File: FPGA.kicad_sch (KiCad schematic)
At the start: 115 parts, among them U7 CAT24C128, U8 LFE5U-25F-8MG285C, U9 W25Q128JVP

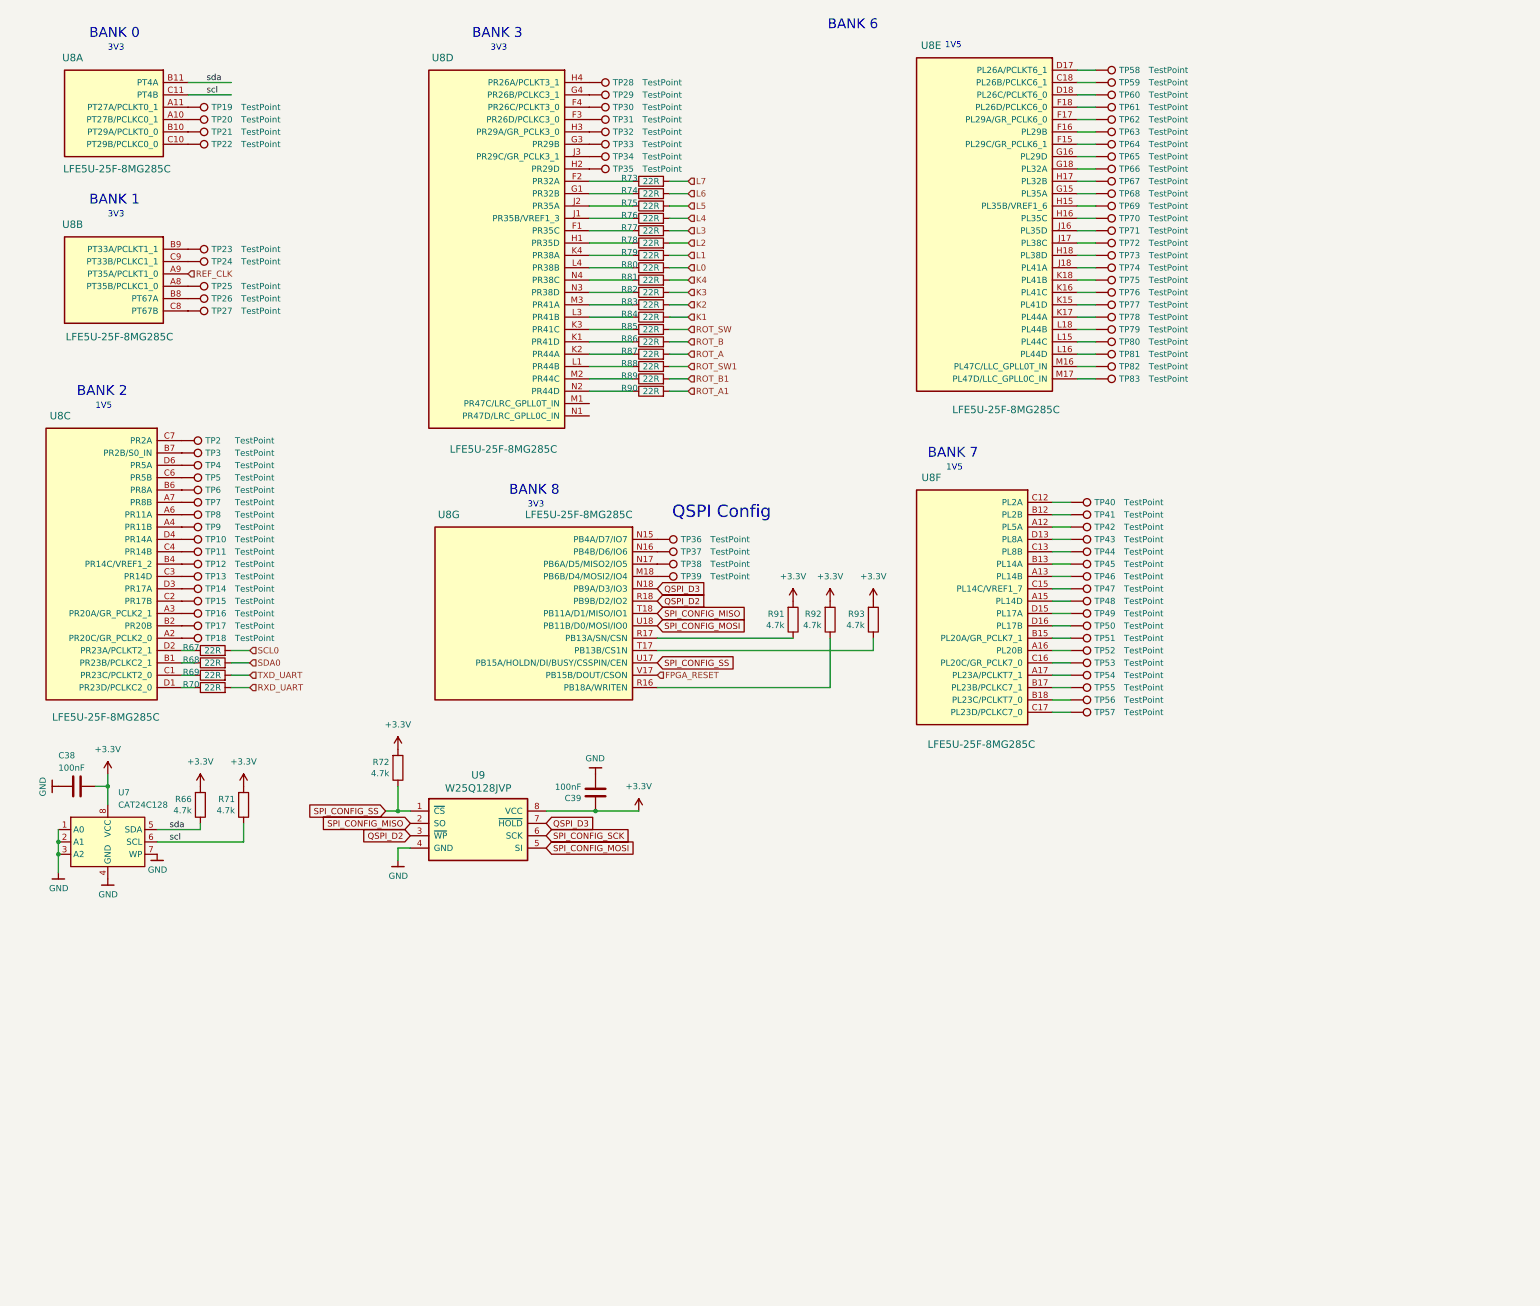
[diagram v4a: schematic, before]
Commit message: Add sram and oscillator 27MHz
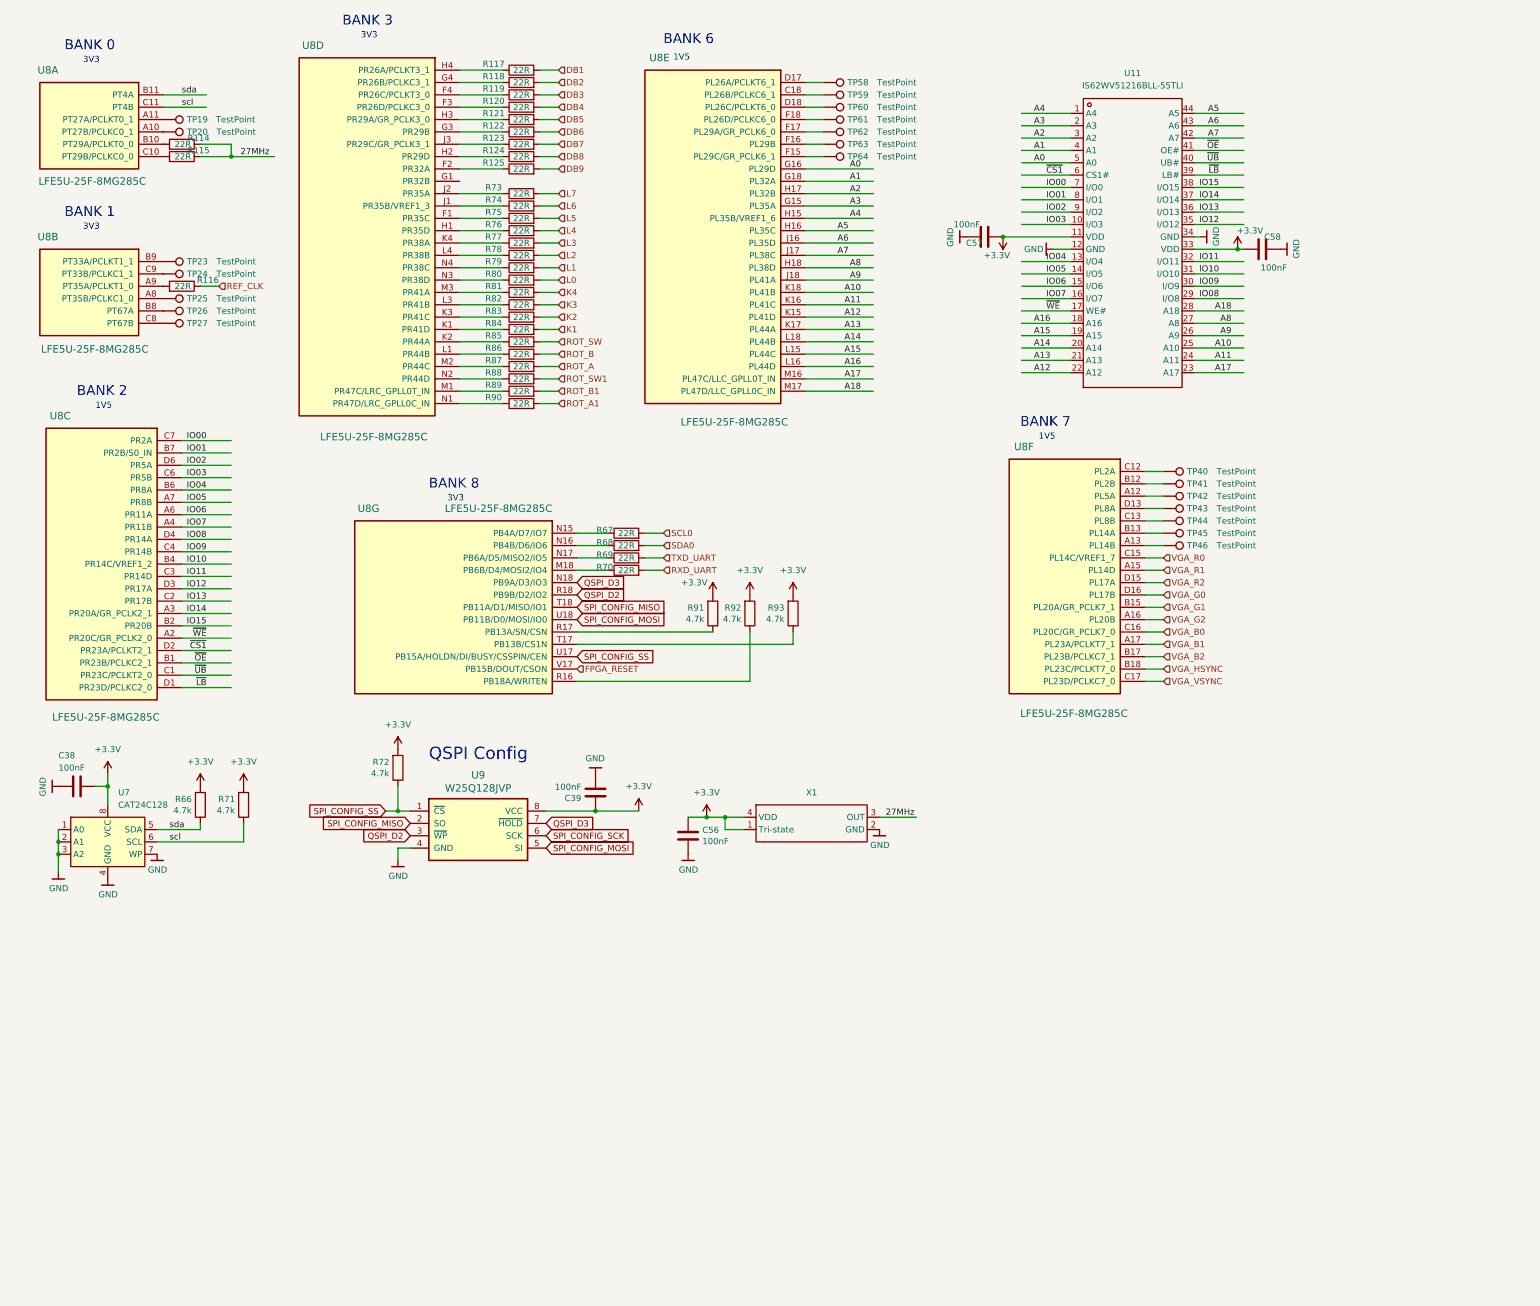
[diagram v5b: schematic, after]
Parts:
- removed TP10, TP11, TP12, TP13, TP14, TP15, TP16, TP17, TP18, TP2, TP21, TP22, TP28, TP29, TP3, TP30, TP31, TP32, TP33, TP34, TP35, TP36, TP37, TP38, TP39, TP4, TP47, TP48, TP49, TP5, TP50, TP51, TP52, TP53, TP54, TP55, TP56, TP57, TP6, TP65, TP66, TP67, TP68, TP69, TP7, TP70, TP71, TP72, TP73, TP74, TP75, TP76, TP77, TP78, TP79, TP8, TP80, TP81, TP82, TP83, TP9: TestPoint, TestPoint:TestPoint_THTPad_D1.5mm_Drill0.7mm, symbol Connector:TestPoint
- added C56, C57, C58: 100nF, Capacitor_SMD:C_0603_1608Metric, symbol Device:C
- added R114, R115, R116, R117, R118, R119, R120, R121, R122, R123, R124, R125: 22R, Resistor_SMD:R_0603_1608Metric, symbol Device:R
- added U11: IS62WV51216BLL-55TLI, EasyEDA_Lib:TSOP-44_L18.4-W10.2-P0.80-LS11.8-BL, symbol EasyEDA_Lib:IS62WV51216BLL-55TLI
- added X1: 27MHz, EasyEDA_Lib:OSC-SMD_4P-L3.2-W2.5-BL, symbol EasyEDA_Lib:OT2EL4C4JI-111OLP-27M
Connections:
- net +3.3V: now also C56.1, C57.1, C58.1, U11.11 (VDD), U11.33 (VDD), X1.1 (Tri-state), X1.4 (VDD)
- net GND: now also C56.2, C57.2, C58.2, U11.12 (GND), U11.34 (GND), X1.2 (GND)
- net REF_CLK: now also R116.1; no longer U8.A9 (PT35A/PCLKT1_0)
- net at U8.B10 (PT29A/PCLKT0_0): now also R114.2
- net at U8.C10 (PT29B/PCLKC0_0): now also R115.2
- net ~{WE}: now reaches U8.A2 (PR20C/GR_PCLK2_0)
- net ~{WE}: now also U11.17 (WE#)
- net IO14: now reaches U8.A3 (PR20A/GR_PCLK2_1)
- net IO14: now also U11.37 (I/O14)
- net IO07: now reaches U8.A4 (PR11B)
- net IO07: now also U11.16 (I/O7)
- net IO06: now reaches U8.A6 (PR11A)
- net IO06: now also U11.15 (I/O6)
- net IO05: now reaches U8.A7 (PR8B)
- net IO05: now also U11.14 (I/O5)
- net at R68.1: now also U8.N16 (PB4B/D6/IO6); no longer U8.B1 (PR23B/PCLKC2_1)
- net IO15: now reaches U8.B2 (PR20B)
- net IO15: now also U11.38 (I/O15)
- net IO10: now reaches U8.B4 (PR14C/VREF1_2)
- net IO10: now also U11.31 (I/O10)
- net IO04: now reaches U8.B6 (PR8A)
- net IO04: now also U11.13 (I/O4)
- net IO01: now reaches U8.B7 (PR2B/S0_IN)
- net IO01: now also U11.8 (I/O1)
- net at R69.1: now also U8.N17 (PB6A/D5/MISO2/IO5); no longer U8.C1 (PR23C/PCLKT2_0)
- net IO13: now reaches U8.C2 (PR17B)
- net IO13: now also U11.36 (I/O13)
- net IO11: now reaches U8.C3 (PR14D)
- net IO11: now also U11.32 (I/O11)
- net IO09: now reaches U8.C4 (PR14B)
- net IO09: now also U11.30 (I/O9)
- net IO03: now reaches U8.C6 (PR5B)
- net IO03: now also U11.10 (I/O3)
- net IO00: now reaches U8.C7 (PR2A)
- net IO00: now also U11.7 (I/O0)
- net at R70.1: now also U8.M18 (PB6B/D4/MOSI2/IO4); no longer U8.D1 (PR23D/PCLKC2_0)
- net at R67.1: now also U8.N15 (PB4A/D7/IO7); no longer U8.D2 (PR23A/PCLKT2_1)
- net IO12: now reaches U8.D3 (PR17A)
- net IO12: now also U11.35 (I/O12)
- net IO08: now reaches U8.D4 (PR14A)
- net IO08: now also U11.29 (I/O8)
- net IO02: now reaches U8.D6 (PR5A)
- net IO02: now also U11.9 (I/O2)
- net at U8.F1 (PR35C): now also R75.1; no longer R77.1
- net at U8.F2 (PR32A): now also R125.1; no longer R73.1
- net at U8.F3 (PR26D/PCLKC3_0): now also R120.1
- net at U8.F4 (PR26C/PCLKT3_0): now also R119.1
- net at U8.G1 (PR32B): no longer R74.1
- net at U8.G3 (PR29B): now also R122.1
- net at U8.G4 (PR26B/PCLKC3_1): now also R118.1
- net at U8.H1 (PR35D): now also R76.1; no longer R78.1
- net at U8.H2 (PR29D): now also R124.1
- net at U8.H3 (PR29A/GR_PCLK3_0): now also R121.1
- net at U8.H4 (PR26A/PCLKT3_1): now also R117.1
- net at U8.J1 (PR35B/VREF1_3): now also R74.1; no longer R76.1
- net at U8.J2 (PR35A): now also R73.1; no longer R75.1
- net at U8.J3 (PR29C/GR_PCLK3_1): now also R123.1
- net at U8.K1 (PR41D): now also R84.1; no longer R86.1
- net at U8.K2 (PR44A): now also R85.1; no longer R87.1
- net at U8.K3 (PR41C): now also R83.1; no longer R85.1
- net at U8.K4 (PR38A): now also R77.1; no longer R79.1
- net at U8.L1 (PR44B): now also R86.1; no longer R88.1
- net at U8.L3 (PR41B): now also R82.1; no longer R84.1
- net at U8.L4 (PR38B): now also R78.1; no longer R80.1
- net at U8.M1 (PR47C/LRC_GPLL0T_IN): now also R89.1
- net at U8.M2 (PR44C): now also R87.1; no longer R89.1
- net at U8.M3 (PR41A): now also R81.1; no longer R83.1
- net at U8.N1 (PR47D/LRC_GPLL0C_IN): now also R90.1
- net at U8.N2 (PR44D): now also R88.1; no longer R90.1
- net at U8.N3 (PR38D): now also R80.1; no longer R82.1
- net at U8.N4 (PR38C): now also R79.1; no longer R81.1
- net A3: now reaches U8.G15 (PL35A)
- net A3: now also U11.2 (A3)
- net A0: now reaches U8.G16 (PL29D)
- net A0: now also U11.5 (A0)
- net A1: now reaches U8.G18 (PL32A)
- net A1: now also U11.4 (A1)
- net A4: now reaches U8.H15 (PL35B/VREF1_6)
- net A4: now also U11.1 (A4)
- net A5: now reaches U8.H16 (PL35C)
- net A5: now also U11.44 (A5)
- net A2: now reaches U8.H17 (PL32B)
- net A2: now also U11.3 (A2)
- net A8: now reaches U8.H18 (PL38D)
- net A8: now also U11.27 (A8)
- net A6: now reaches U8.J16 (PL35D)
- net A6: now also U11.43 (A6)
- net A7: now reaches U8.J17 (PL38C)
- net A7: now also U11.42 (A7)
- net A9: now reaches U8.J18 (PL41A)
- net A9: now also U11.26 (A9)
- net A12: now reaches U8.K15 (PL41D)
- net A12: now also U11.22 (A12)
- net A11: now reaches U8.K16 (PL41C)
- net A11: now also U11.24 (A11)
- net A13: now reaches U8.K17 (PL44A)
- net A13: now also U11.21 (A13)
- net A10: now reaches U8.K18 (PL41B)
- net A10: now also U11.25 (A10)
- net A15: now reaches U8.L15 (PL44C)
- net A15: now also U11.19 (A15)
- net A16: now reaches U8.L16 (PL44D)
- net A16: now also U11.18 (A16)
- net A14: now reaches U8.L18 (PL44B)
- net A14: now also U11.20 (A14)
- net A17: now reaches U8.M16 (PL47C/LLC_GPLL0T_IN)
- net A17: now also U11.23 (A17)
- net A18: now reaches U8.M17 (PL47D/LLC_GPLL0C_IN)
- net A18: now also U11.28 (A18)
- net VGA_R1: now reaches U8.A15 (PL14D)
- net VGA_G2: now reaches U8.A16 (PL20B)
- net VGA_B1: now reaches U8.A17 (PL23A/PCLKT7_1)
- net VGA_G1: now reaches U8.B15 (PL20A/GR_PCLK7_1)
- net VGA_B2: now reaches U8.B17 (PL23B/PCLKC7_1)
- net VGA_HSYNC: now reaches U8.B18 (PL23C/PCLKT7_0)
- net VGA_R0: now reaches U8.C15 (PL14C/VREF1_7)
- net VGA_B0: now reaches U8.C16 (PL20C/GR_PCLK7_0)
- net VGA_VSYNC: now reaches U8.C17 (PL23D/PCLKC7_0)
- net VGA_R2: now reaches U8.D15 (PL17A)
- net VGA_G0: now reaches U8.D16 (PL17B)
- new net: R116.2, U8.A9 (PT35A/PCLKT1_0)
- new net 27MHz: R114.1, R115.1, X1.3 (OUT)
- new net DB1: R117.2
- new net DB2: R118.2
- new net DB3: R119.2
- new net DB4: R120.2
- new net DB5: R121.2
- new net DB6: R122.2
- new net DB7: R123.2
- new net DB8: R124.2
- new net DB9: R125.2
- new net ~{CS1}: U11.6 (CS1#), U8.D2 (PR23A/PCLKT2_1)
- new net ~{LB}: U11.39 (LB#), U8.D1 (PR23D/PCLKC2_0)
- new net ~{OE}: U11.41 (OE#), U8.B1 (PR23B/PCLKC2_1)
- new net ~{UB}: U11.40 (UB#), U8.C1 (PR23C/PCLKT2_0)
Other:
- moved on the sheet: R67, R68, R69, R70, R73, R74, R75, R76, R77, R78, R79, R80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

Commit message: Routing sram
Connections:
- net A2: now also U8.F18 (PL26D/PCLKC6_0); no longer U8.H17 (PL32B)
- net A3: no longer U8.G15 (PL35A)
- net A4: now also U8.A17 (PL23A/PCLKT7_1); no longer U8.H15 (PL35B/VREF1_6)
- net A6: now also U8.B17 (PL23B/PCLKC7_1); no longer U8.J16 (PL35D)
- net A7: now also U8.B15 (PL20A/GR_PCLK7_1); no longer U8.J17 (PL38C)
- net IO13: now also U8.G15 (PL35A); no longer U8.C2 (PR17B)
- net IO14: now also U8.F15 (PL29C/GR_PCLK6_1); no longer U8.A3 (PR20A/GR_PCLK2_1)
- net IO15: now also U8.D16 (PL17B); no longer U8.B2 (PR20B)
- net VGA_B0: no longer U8.C16 (PL20C/GR_PCLK7_0)
- net VGA_B1: no longer U8.A17 (PL23A/PCLKT7_1)
- net VGA_B2: no longer U8.B17 (PL23B/PCLKC7_1)
- net VGA_G0: no longer U8.D16 (PL17B)
- net VGA_G1: no longer U8.B15 (PL20A/GR_PCLK7_1)
- net VGA_G2: no longer U8.A16 (PL20B)
- net VGA_HSYNC: no longer U8.B18 (PL23C/PCLKT7_0)
- net VGA_R0: no longer U8.C15 (PL14C/VREF1_7)
- net VGA_R1: no longer U8.A15 (PL14D)
- net VGA_R2: no longer U8.D15 (PL17A)
- net VGA_VSYNC: no longer U8.C17 (PL23D/PCLKC7_0)
- net ~{LB}: now also U8.D15 (PL17A); no longer U8.D1 (PR23D/PCLKC2_0)
- net ~{OE}: now also U8.C15 (PL14C/VREF1_7); no longer U8.B1 (PR23B/PCLKC2_1)
- net ~{UB}: now also U8.C16 (PL20C/GR_PCLK7_0); no longer U8.C1 (PR23C/PCLKT2_0)
- net at U8.C18 (PL26B/PCLKC6_1): no longer TP59.1
- net at U8.D17 (PL26A/PCLKT6_1): no longer TP58.1
- net at U8.D18 (PL26C/PCLKT6_0): no longer TP60.1
- net at TP64.1: no longer U8.F15 (PL29C/GR_PCLK6_1)
- net at U8.F16 (PL29B): no longer TP63.1
- net at U8.F17 (PL29A/GR_PCLK6_0): no longer TP62.1
- net at TP61.1: no longer U8.F18 (PL26D/PCLKC6_0)
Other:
- moved on the sheet: TP58, TP59, TP60, TP61, TP62, TP63, TP64
